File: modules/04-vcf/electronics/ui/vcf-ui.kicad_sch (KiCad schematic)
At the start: 39 parts, among them J1 Conn_02x03_Odd_Even, J2 Conn_02x02_Counter_Clockwise, J4 Conn_01x02, J5 Conn_01x06, J6 Conn_02x04_Odd_Even, U1 TL072

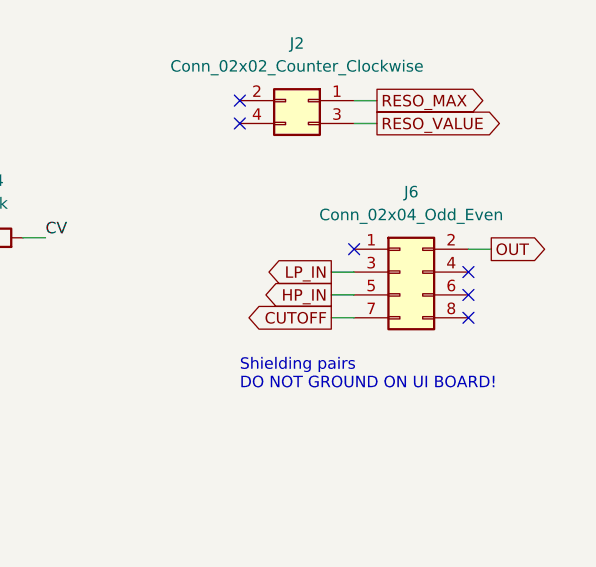
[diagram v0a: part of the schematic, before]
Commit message: Fixed VCF connector positions
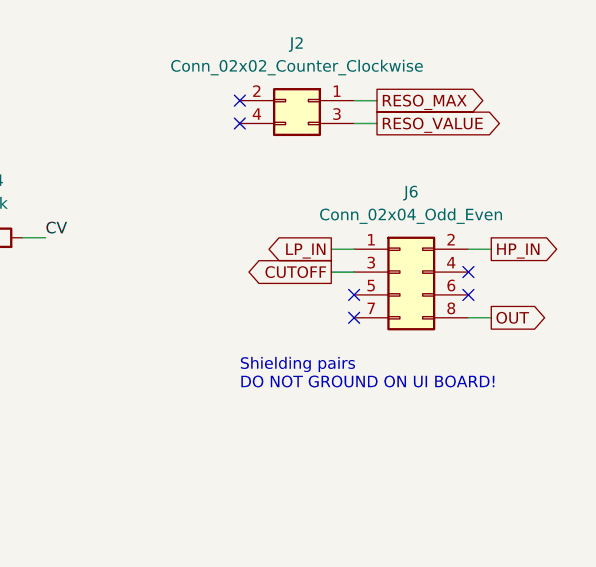
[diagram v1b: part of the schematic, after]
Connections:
- net CUTOFF: now also J6.3 (Pin_3); no longer J6.7 (Pin_7)
- net HP_IN: now also J6.2 (Pin_2); no longer J6.5 (Pin_5)
- net LP_IN: now also J6.1 (Pin_1); no longer J6.3 (Pin_3)
- net OUT: now also J6.8 (Pin_8); no longer J6.2 (Pin_2)

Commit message: Added VCF full BOM
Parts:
- C1, C2: Part URL (none) -> https://mou.sr/4adMnbf; Part no. (none) -> 594-K104K15X7RF53L2; Vendor (none) -> Mouser
- J6: Part URL (none) -> https://mou.sr/4qqxl75; Part no. (none) -> 200-SSW10401TD; Vendor (none) -> Mouser
- RV_CUTOFF_BIAS1: Part URL (none) -> https://mou.sr/44pTlq5; Part no. (none) -> 774-06TR4AA103CP; Vendor (none) -> Mouser
- U1: Part URL (none) -> https://mou.sr/48zN39J; Part no. (none) -> 595-TL072CP; Vendor (none) -> Mouser
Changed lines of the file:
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@@
 			)
 		)
+		(property "Part URL" "https://mou.sr/4adMnbf"
+			(at 231.14 44.45 0)
+			(effects
+				(font
+					(size 1.27 1.27)
+				)
+				(hide yes)
+			)
+		)
+		(property "Part no." "594-K104K15X7RF53L2"
+			(at 231.14 44.45 0)
+			(effects
+				(font
+					(size 1.27 1.27)
+				)
+				(hide yes)
+			)
+		)
+		(property "Vendor" "Mouser"
+			(at 231.14 44.45 0)
+			(effects
+				(font
+					(size 1.27 1.27)
+				)
+				(hide yes)
+			)
+		)
 		(pin "1"
 		)
@@
 			)
 		)
+		(property "Part URL" "https://mou.sr/48zN39J"
+			(at 90.17 99.06 0)
+			(effects
+				(font
+					(size 1.27 1.27)
+				)
+				(hide yes)
+			)
+		)
+		(property "Part no." "595-TL072CP"
+			(at 90.17 99.06 0)
+			(effects
+				(font
+					(size 1.27 1.27)
+				)
+				(hide yes)
+			)
+		)
+		(property "Vendor" "Mouser"
+			(at 90.17 99.06 0)
+			(effects
+				(font
+					(size 1.27 1.27)
+				)
+				(hide yes)
+			)
+		)
 		(pin "3"
 		)
@@
 			)
 		)
-		(property "Part URL" ""
+		(property "Part URL" "https://mou.sr/44pTlq5"
 			(at 45.72 43.18 0)
 			(effects
@@
 			)
 		)
-		(property "Vendor" ""
+		(property "Vendor" "Mouser"
 			(at 45.72 43.18 0)
 			(effects
@@
 			)
 		)
+		(property "Part no." "774-06TR4AA103CP"
+			(at 45.72 43.18 0)
+			(effects
+				(font
+					(size 1.27 1.27)
+				)
+				(hide yes)
+			)
+		)
 		(pin "1"
 		)
@@
 			)
 		)
+		(property "Part URL" "https://mou.sr/48zN39J"
+			(at 224.79 40.64 0)
+			(effects
+				(font
+					(size 1.27 1.27)
+				)
+				(hide yes)
+			)
+		)
+		(property "Part no." "595-TL072CP"
+			(at 224.79 40.64 0)
+			(effects
+				(font
+					(size 1.27 1.27)
+				)
+				(hide yes)
+			)
+		)
+		(property "Vendor" "Mouser"
+			(at 224.79 40.64 0)
+			(effects
+				(font
+					(size 1.27 1.27)
+				)
+				(hide yes)
+			)
+		)
 		(pin "3"
 		)
@@
 			)
 		)
+		(property "Part URL" "https://mou.sr/4adMnbf"
+			(at 231.14 36.83 0)
+			(effects
+				(font
+					(size 1.27 1.27)
+				)
+				(hide yes)
+			)
+		)
+		(property "Part no." "594-K104K15X7RF53L2"
+			(at 231.14 36.83 0)
+			(effects
+				(font
+					(size 1.27 1.27)
+				)
+				(hide yes)
+			)
+		)
+		(property "Vendor" "Mouser"
+			(at 231.14 36.83 0)
+			(effects
+				(font
+					(size 1.27 1.27)
+				)
+				(hide yes)
+			)
+		)
 		(pin "1"
 		)
@@
 			)
 		)
-		(property "Part URL" ""
+		(property "Part URL" "https://mou.sr/4qqxl75"
 			(at 264.16 102.87 0)
 			(effects
@@
 			)
 		)
-		(property "Vendor" ""
+		(property "Vendor" "Mouser"
 			(at 264.16 102.87 0)
 			(effects
@@
 			)
 		)
+		(property "Part no." "200-SSW10401TD"
+			(at 264.16 102.87 0)
+			(effects
+				(font
+					(size 1.27 1.27)
+				)
+				(hide yes)
+			)
+		)
 		(pin "4"
 		)
@@
 			(at 199.39 99.06 0)
 			(effects
+				(font
+					(size 1.27 1.27)
+				)
+				(hide yes)
+			)
+		)
+		(property "Part URL" "https://mou.sr/48zN39J"
+			(at 199.39 99.06 0)
+			(effects
+				(font
+					(size 1.27 1.27)
+				)
+				(hide yes)
+			)
+		)
+		(property "Part no." "595-TL072CP"
+			(at 199.39 99.06 0)
+			(effects
+				(font
+					(size 1.27 1.27)
+				)
+				(hide yes)
+			)
+		)
+		(property "Vendor" "Mouser"
+			(at 199.39 99.06 0)
+			(effects

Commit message: Fixed UI component part number bugs
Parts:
- RV_CUTOFF1, RV_CUTOFF2, RV_MAIN_CUTOFF1, RV_RESO1: Part URL https://mou.sr/4694GMU -> https://mou.sr/41lYe2k; Part no. 652-PTV09A4025FB104 -> 652-PTV09A4025UB104
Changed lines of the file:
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@@
 			)
 		)
-		(property "Part URL" "https://mou.sr/4694GMU"
+		(property "Part URL" "https://mou.sr/41lYe2k"
 			(at 176.53 43.18 0)
 			(effects
@@
 			)
 		)
-		(property "Part no." "652-PTV09A4025FB104"
+		(property "Part no." "652-PTV09A4025UB104"
 			(at 176.53 43.18 0)
 			(effects
@@
 			)
 		)
-		(property "Part URL" "https://mou.sr/4694GMU"
+		(property "Part URL" "https://mou.sr/41lYe2k"
 			(at 161.29 107.95 0)
 			(effects
@@
 			)
 		)
-		(property "Part no." "652-PTV09A4025FB104"
+		(property "Part no." "652-PTV09A4025UB104"
 			(at 161.29 107.95 0)
 			(effects
@@
 			)
 		)
-		(property "Part URL" "https://mou.sr/4694GMU"
+		(property "Part URL" "https://mou.sr/41lYe2k"
 			(at 92.71 41.91 0)
 			(effects
@@
 			)
 		)
-		(property "Part no." "652-PTV09A4025FB104"
+		(property "Part no." "652-PTV09A4025UB104"
 			(at 92.71 41.91 0)
 			(effects
@@
 			)
 		)
-		(property "Part URL" "https://mou.sr/4694GMU"
+		(property "Part URL" "https://mou.sr/41lYe2k"
 			(at 52.07 107.95 0)
 			(effects
@@
 			)
 		)
-		(property "Part no." "652-PTV09A4025FB104"
+		(property "Part no." "652-PTV09A4025UB104"
 			(at 52.07 107.95 0)
 			(effects

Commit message: Updated UI BOMs
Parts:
- R9: Part URL https://mou.sr/46cEvF7 -> https://mou.sr/4hEwI4G; Part no. 603-MFR-25FRF52-220K -> 603-MFR-25FRF52100K
- RV_CUTOFF1, RV_CUTOFF2, RV_MAIN_CUTOFF1, RV_RESO1: Note (none) -> Knurled Shaft

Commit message: KiCAD version update - VCF
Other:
- title: Hog Moduleur VCO UI -> Moduleur VCF UI
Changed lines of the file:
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@@
 	(paper "A4")
 	(title_block
-		(title "Hog Moduleur VCO UI")
-		(date "2025-07-06")
-		(rev "v0.2")
+		(title "Moduleur VCF UI")
+		(date "2026-02-21")
+		(rev "v1.0")
 		(company "Shmøergh")
 	)
